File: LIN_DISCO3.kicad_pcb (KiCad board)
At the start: 2 copper layers, 48.9 x 34.9 mm, 20 parts, among them J1 CAR_STAT, J2 CAR_BAT, J3 WEBASTO, U1 PIC16F628-xxISO, U2 MCP1804x-5002xMB, U3 Si9243A

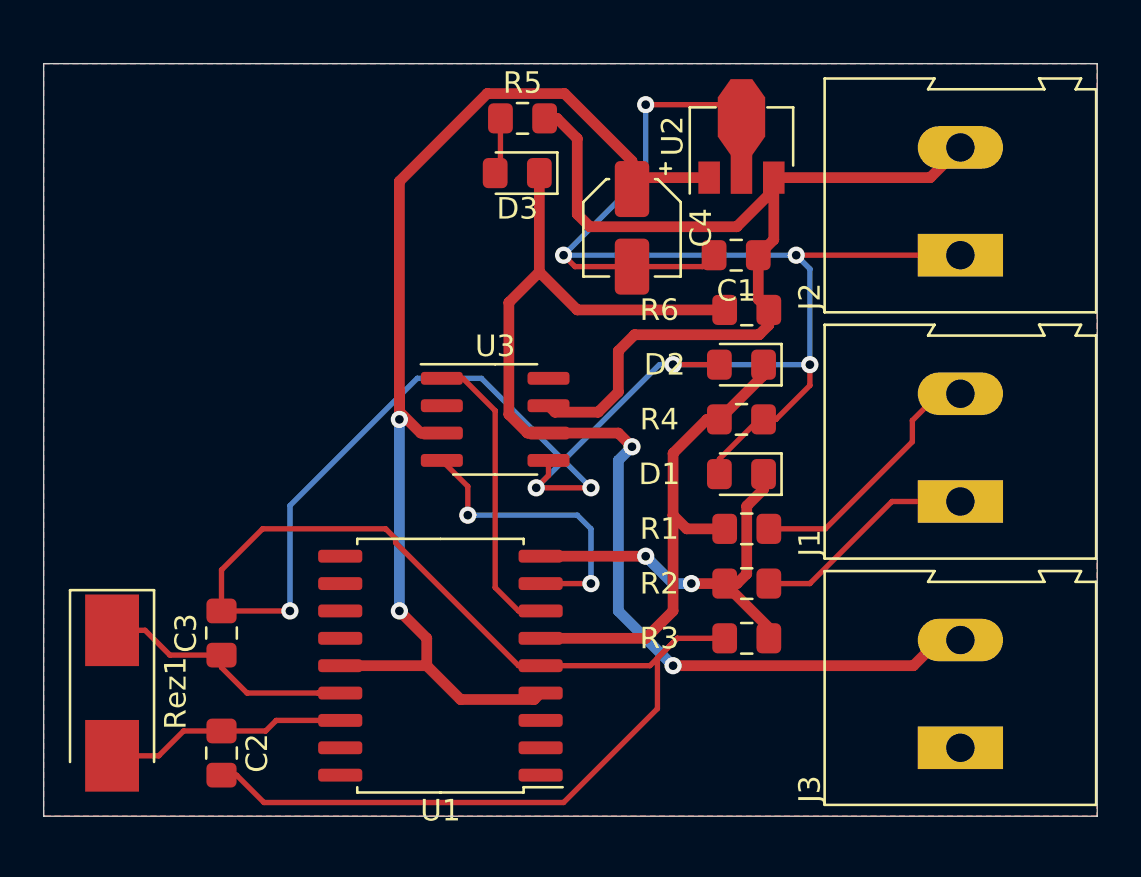
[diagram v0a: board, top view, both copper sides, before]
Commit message: reroute, added 6p arks
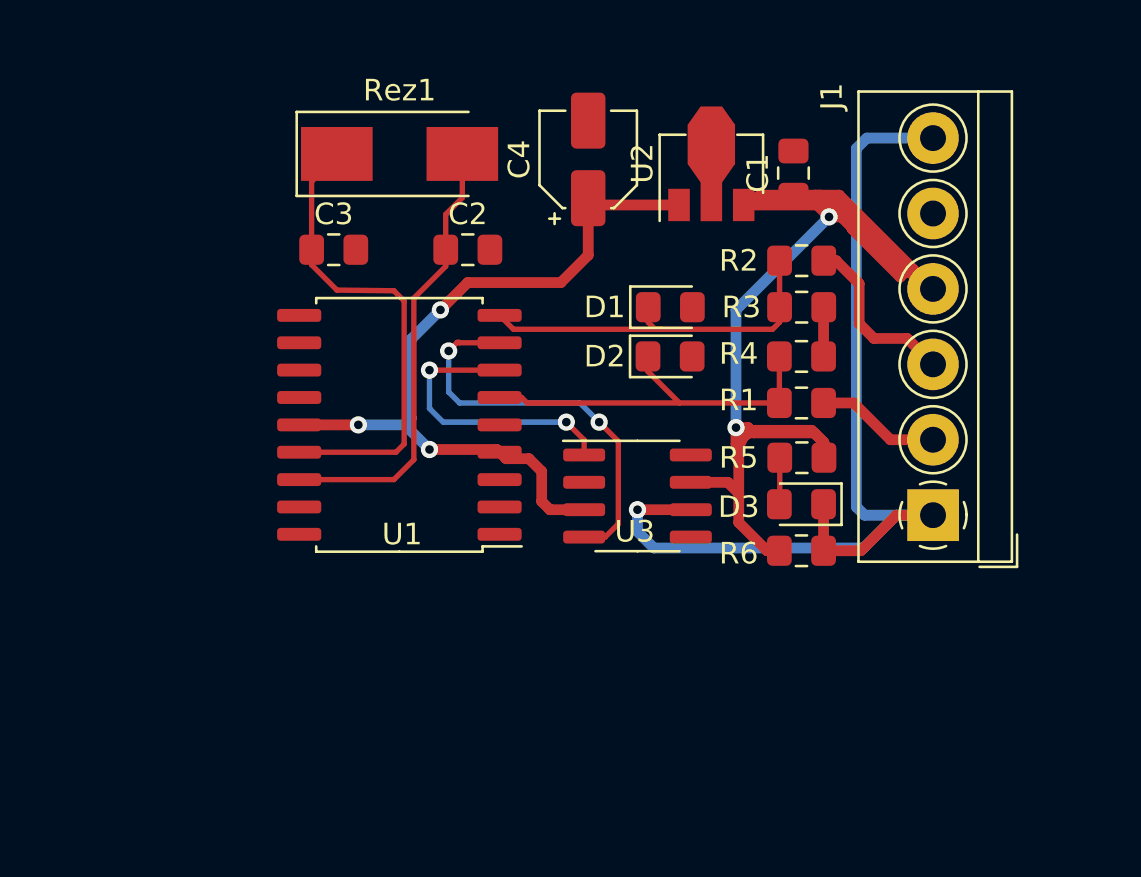
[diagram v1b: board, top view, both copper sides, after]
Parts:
- removed J2: CAR_BAT, TerminalBlock:TerminalBlock_Altech_AK300-2_P5.00mm
- removed J3: WEBASTO, TerminalBlock:TerminalBlock_Altech_AK300-2_P5.00mm
- J1: value CAR_STAT -> Conn_01x06_Female; footprint TerminalBlock:TerminalBlock_Altech_AK300-2_P5.00mm -> TerminalBlock_4Ucon:TerminalBlock_4Ucon_1x06_P3.50mm_Horizontal
- moved Rez1 28.4 mm to (165.7, 61.3), turned to 0 degrees
- moved C2 26.0 mm to (168.9, 65.8), turned to 0 degrees
- moved R5 20.4 mm to (184.4, 75.4)
- moved D3 20.3 mm to (184.4, 77.6)
- moved C3 18.5 mm to (162.7, 65.8), turned to 0 degrees
- moved R3 15.6 mm to (184.4, 68.5), turned to 0 degrees
- moved R2 15.2 mm to (184.4, 66.3)
- moved R6 11.5 mm to (184.4, 79.8), turned to 180 degrees
- moved U1 11.3 mm to (165.7, 73.9)
- moved D1 8.42 mm to (178.3, 68.5), turned to 0 degrees
- moved U3 7.50 mm to (176.8, 77.2)
- moved R1 6.37 mm to (184.4, 72.9)
- moved C1 4.65 mm to (184.0, 62.2), turned to 90 degrees
- moved R4 4.04 mm to (184.4, 70.7)
- moved C4 3.77 mm to (174.5, 61.6), turned to 90 degrees
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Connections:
- D1 pad 1: IGNITION -> RB3
- D2 pad 1: LOW_BEAM -> RB0
- J1 pad 1: Net-(J1-Pad1) -> WBUS
- J1 pad 2: Net-(J1-Pad2) -> LOW_BEAM
- R1 pad 1: LOW_BEAM -> RB0
- R1 pad 2: Net-(J1-Pad2) -> LOW_BEAM
- R2 pad 1: IGNITION -> RB3
- R2 pad 2: Net-(J1-Pad1) -> IGNITION
- R3 pad 1: IGNITION -> RB3
- R4 pad 1: LOW_BEAM -> RB0
- U1 pad 6: LOW_BEAM -> RB0
- U1 pad 9: IGNITION -> RB3
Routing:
- net GND: track 155.1 -> 6.29 mm, vias 8 -> 0
- net Vcc: track 55.2 -> 36.6 mm, vias 2 -> 3
- net RB0: track 0.00 -> 18.0 mm
- net RB3: track 0.00 -> 17.7 mm
- net LOW_BEAM: track 22.8 -> 5.79 mm
- net VBAT: track 45.8 -> 59.9 mm, vias 0 -> 2
- net Net-(J1-Pad2): track 12.1 -> 0.00 mm
- net IGNITION: track 18.6 -> 8.15 mm, vias 2 -> 0
- net Net-(J1-Pad1): track 10.5 -> 0.00 mm
- net Net-(C3-Pad1): track 12.1 -> 22.3 mm
- net Net-(C2-Pad1): track 11.3 -> 20.8 mm
- net WLINE_TX: track 13.9 -> 18.9 mm
- net WBUS: track 52.8 -> 50.2 mm, vias 2 -> 1
- net WLINE_RX: track 13.9 -> 13.5 mm, vias 0 -> 2
- removed copper zone on B.Cu, net GND
- removed copper zone on F.Cu, net GND
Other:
- board outline removed

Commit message: reroute: voltages
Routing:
- net GND: track 6.29 -> 113.0 mm, vias 0 -> 4
- net WBUS: track 50.2 -> 48.2 mm
- net Vcc: track 36.6 -> 37.6 mm
- added copper zone on B.Cu, net GND
- added copper zone on F.Cu, net GND
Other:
- board outline added: 35.6 x 22.6 mm

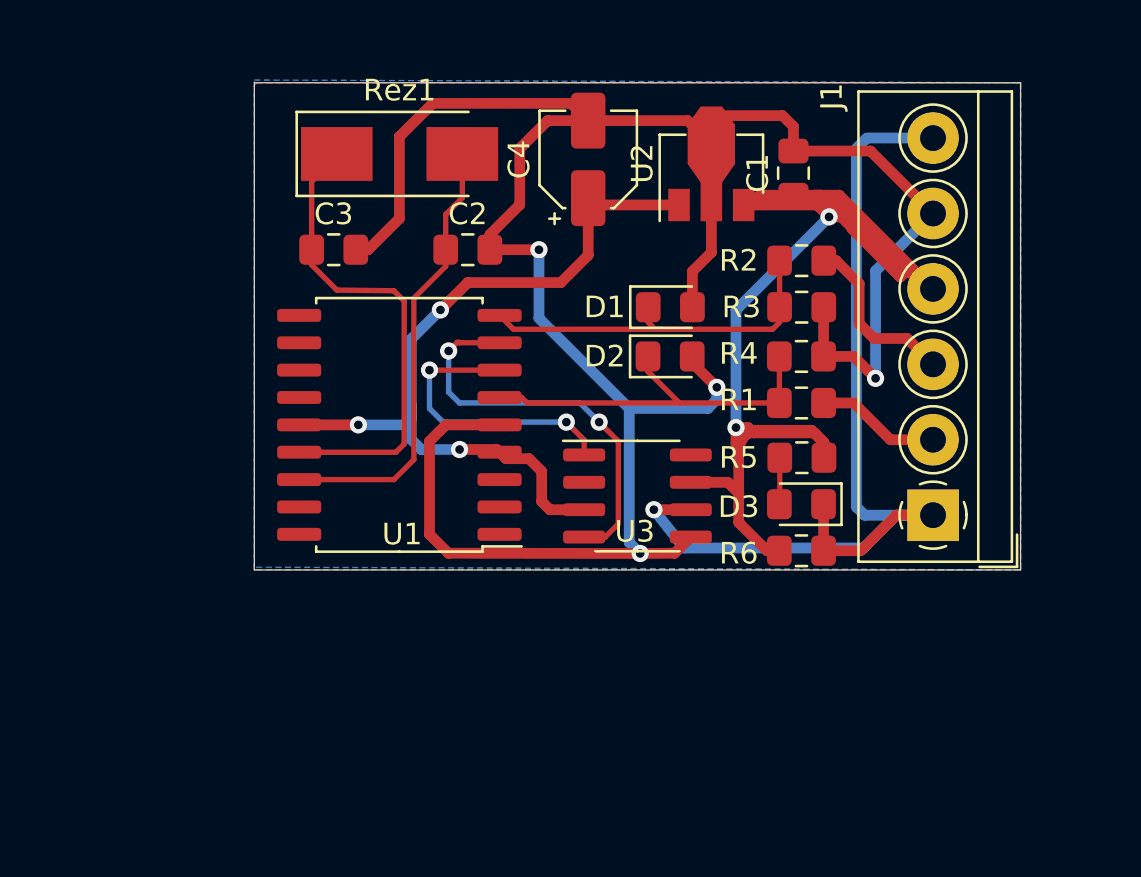
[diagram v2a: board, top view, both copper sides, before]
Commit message: added ICSP port
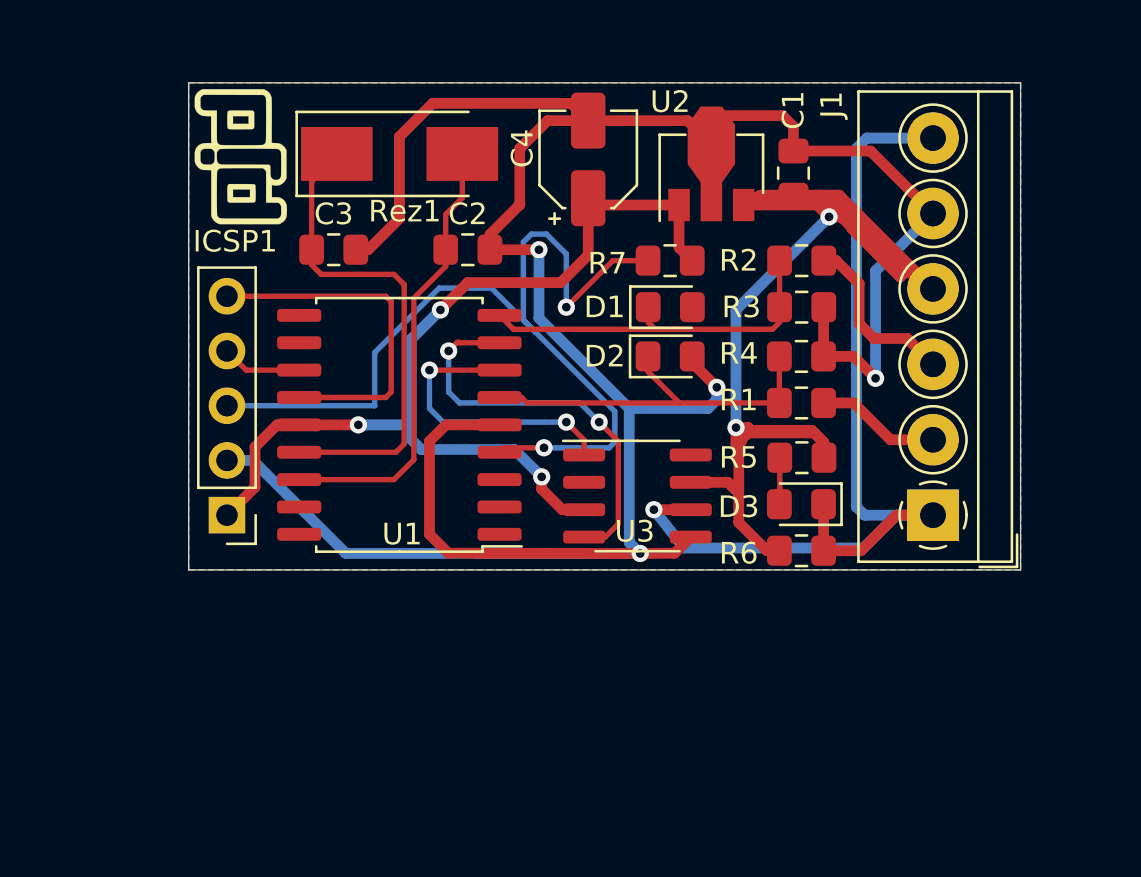
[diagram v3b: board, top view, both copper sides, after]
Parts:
- added G***: LOGO, logo:pjd_icon, F.Cu at (158.4, 61.5)
- added ICSP1: Conn_01x05_Male, Connector_PinHeader_2.54mm:PinHeader_1x05_P2.54mm_Vertical, F.Cu at (157.7, 78.1)
- added R7: 10k, Resistor_SMD:R_0805_2012Metric_Pad1.15x1.40mm_HandSolder, F.Cu at (178.3, 66.3)
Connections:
- U1 pad 12: Net-(U1-Pad12) -> CLK
- U1 pad 13: Net-(U1-Pad13) -> DATA_IO
- U1 pad 4: Vcc -> Vpp
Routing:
- net Vpp: track 0.00 -> 45.1 mm, vias 0 -> 2
- net DATA_IO: track 0.00 -> 16.3 mm
- net GND: track 113.0 -> 128.7 mm
- net Vcc: track 37.6 -> 46.2 mm
- net CLK: track 0.00 -> 3.72 mm
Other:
- board size 35.6 x 22.6 mm -> 38.6 x 22.6 mm
- board text added: "26.01.22"
- board text added: "CLK"
- board text added: "DATA_IO"
- board text added: "GND"
- board text added: "Gnd"
- board text added: "IGNITION"
- board text added: "LOW_BEAM"
- board text added: "VBAT"
- board text added: "Vcc"
- board text added: "Vpp"
- board text added: "WBUS"

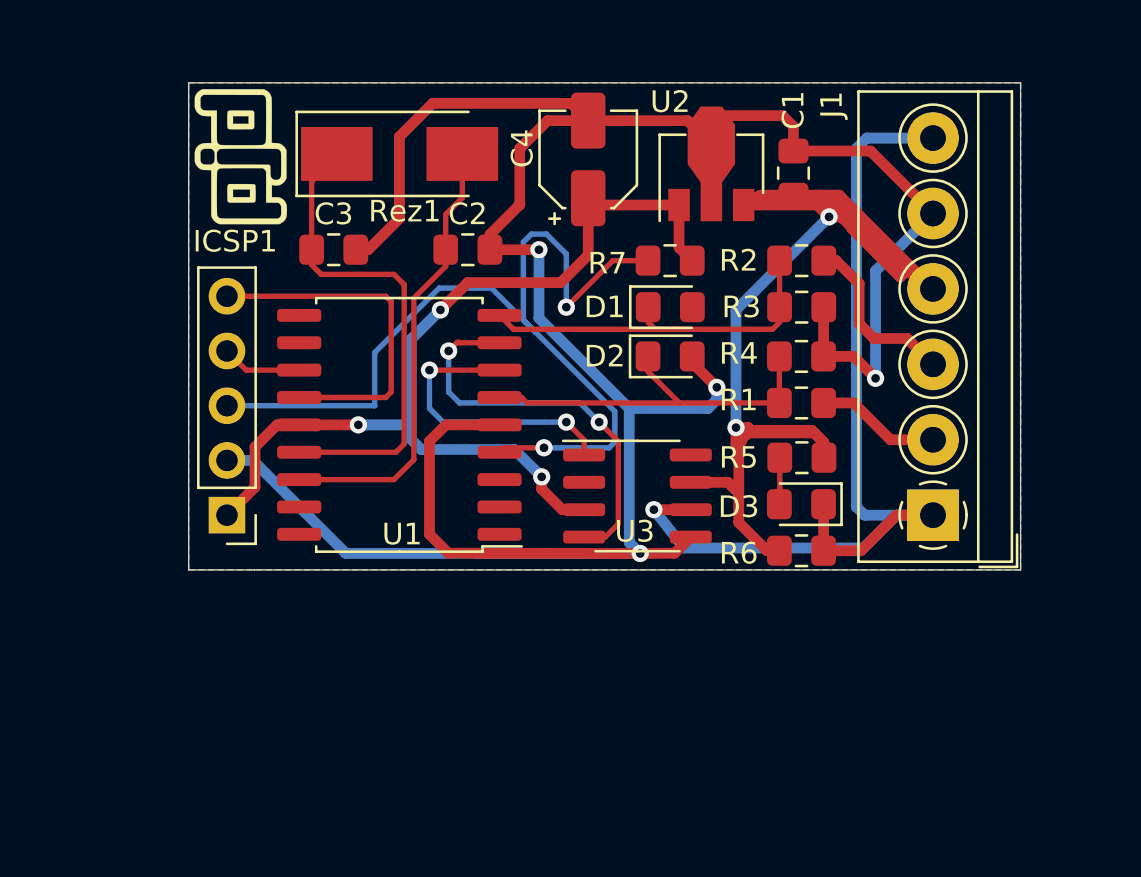
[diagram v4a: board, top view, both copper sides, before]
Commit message: updated board for sot23 and miniMELF
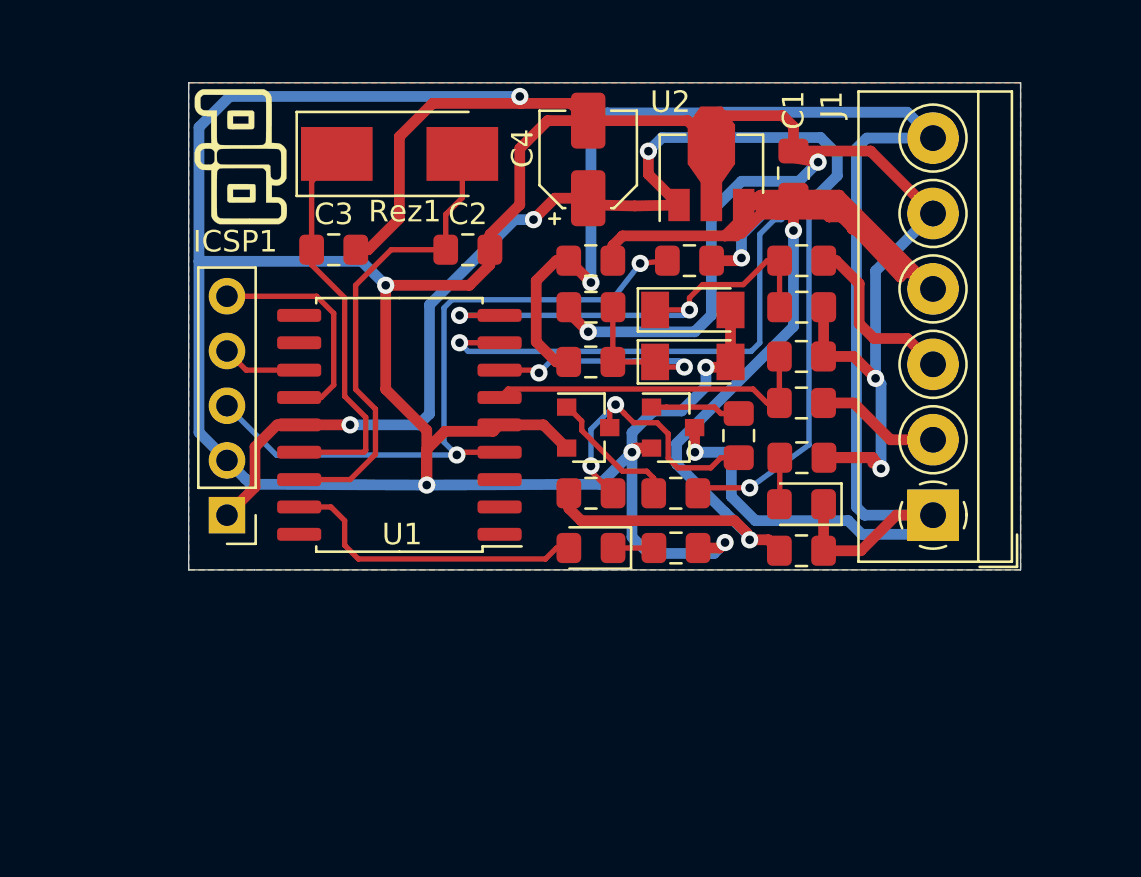
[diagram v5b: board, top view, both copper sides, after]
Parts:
- removed D2: D_Zener_5V6, Diode_SMD:D_0805_2012Metric_Pad1.15x1.40mm_HandSolder
- removed U3: Si9243A, Package_SO:SOIC-8_3.9x4.9mm_P1.27mm
- added D4: D_Zener_5V6, Diode_SMD:D_MiniMELF, F.Cu at (179.4, 71.0)
- added D5: LED, LED_SMD:LED_0805_2012Metric_Pad1.15x1.40mm_HandSolder, F.Cu at (174.6, 79.6)
- added Q1: BC847, Package_TO_SOT_SMD:SOT-23, F.Cu at (174.5, 74.0)
- added Q2: BC847, Package_TO_SOT_SMD:SOT-23, F.Cu at (178.4, 74.0)
- added R10: 10K, Resistor_SMD:R_0805_2012Metric_Pad1.15x1.40mm_HandSolder, F.Cu at (181.5, 74.4)
- added R11: 10k, Resistor_SMD:R_0805_2012Metric_Pad1.15x1.40mm_HandSolder, F.Cu at (174.6, 71.0)
- added R12: 10K, Resistor_SMD:R_0805_2012Metric_Pad1.15x1.40mm_HandSolder, F.Cu at (174.6, 66.3)
- added R13: 2K, Resistor_SMD:R_0805_2012Metric_Pad1.15x1.40mm_HandSolder, F.Cu at (178.6, 79.6)
- added R6: 10K, Resistor_SMD:R_0805_2012Metric_Pad1.15x1.40mm_HandSolder, F.Cu at (178.6, 77.1)
- added R8: 10K, Resistor_SMD:R_0805_2012Metric_Pad1.15x1.40mm_HandSolder, F.Cu at (174.6, 77.1)
- added R9: 10k, Resistor_SMD:R_0805_2012Metric_Pad1.15x1.40mm_HandSolder, F.Cu at (174.6, 68.5)
- D1: footprint Diode_SMD:D_0805_2012Metric_Pad1.15x1.40mm_HandSolder -> Diode_SMD:D_MiniMELF
- moved D1 1.05 mm to (179.4, 68.6)
- moved R7 0.90 mm to (179.2, 66.3)
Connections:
- R5 pad 2: VBAT -> GND
- U1 pad 17: Net-(U1-Pad17) -> W_ACTIVE
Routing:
- net GND: track 128.7 -> 199.2 mm, vias 4 -> 10
- net WBUS: track 48.2 -> 79.2 mm, vias 1 -> 2
- net WLINE_TX: track 18.9 -> 40.3 mm
- net VBAT: track 59.9 -> 76.1 mm
- net W_ACTIVE: track 0.00 -> 14.4 mm
- net Net-(Q1-Pad3): track 0.00 -> 13.8 mm, vias 0 -> 2
- net Vpp: track 45.1 -> 32.1 mm
- net Vcc: track 46.2 -> 52.9 mm, vias 3 -> 4
- net Net-(Q1-Pad1): track 0.00 -> 6.36 mm
- net DATA_IO: track 16.3 -> 10.5 mm
- net Net-(C3-Pad1): track 22.7 -> 18.4 mm
- net RB3: track 17.7 -> 21.8 mm, vias 0 -> 2
- net Net-(Q2-Pad1): track 0.00 -> 4.04 mm
- net WLINE_RX: track 13.5 -> 17.2 mm
- net RB0: track 18.0 -> 15.6 mm
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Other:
- board text added: "15.02.22"
- board text removed: "26.01.22"

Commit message: board layout prepared for production
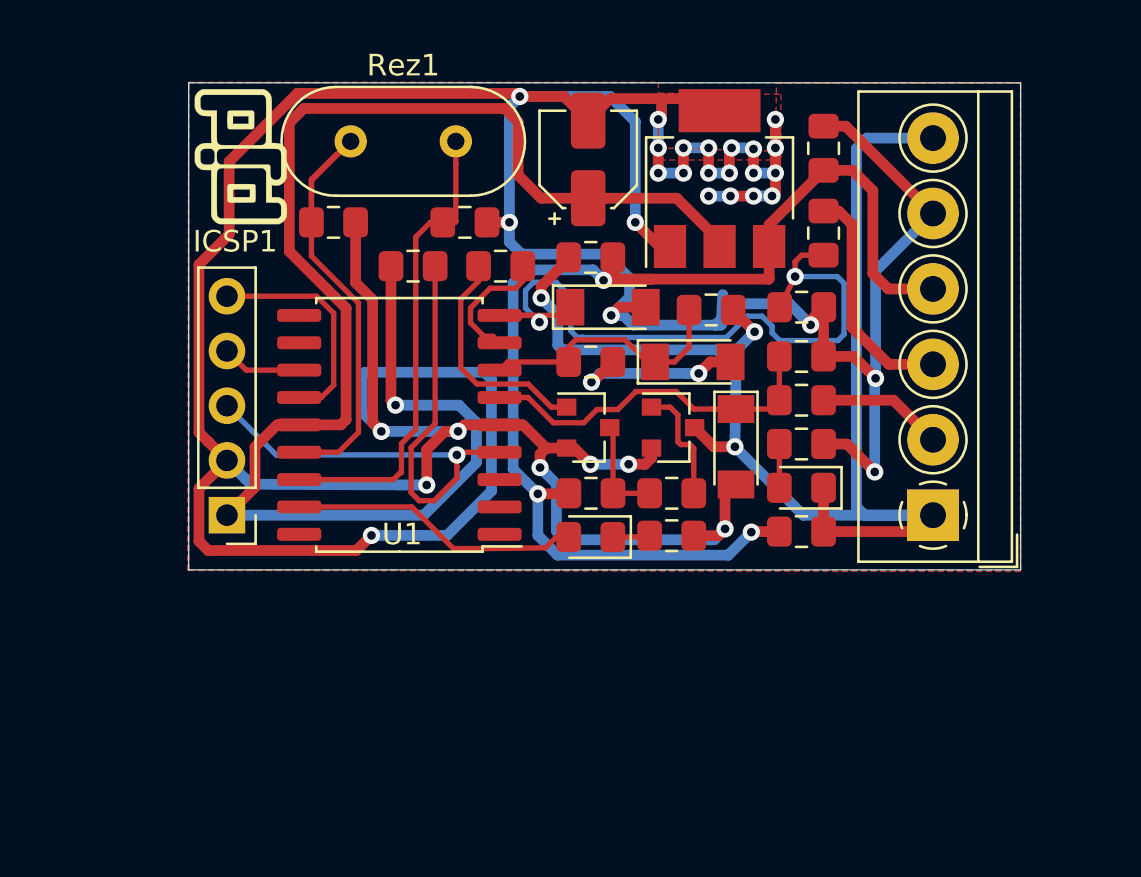
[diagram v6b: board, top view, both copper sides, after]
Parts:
- added D2: D_Zener_5V6, Diode_SMD:D_MiniMELF, F.Cu at (181.4, 74.9)
- Rez1: footprint Crystal:Crystal_SMD_0603-2Pin_6.0x3.5mm_HandSoldering -> Crystal:Crystal_HC49-U_Vertical
- U2: value MCP1804x-5002xMB -> MCP1754S-5002xCB; footprint Package_TO_SOT_SMD:SOT-89-3 -> Package_TO_SOT_SMD:SOT-223
- moved R6 13.3 mm to (170.4, 66.5)
- moved R7 12.8 mm to (166.4, 66.5), turned to 0 degrees
- moved R11 6.09 mm to (180.2, 68.6), turned to 180 degrees
- moved R10 4.10 mm to (178.4, 77.1), turned to 180 degrees
- moved D1 3.94 mm to (175.4, 68.5)
- moved R9 2.54 mm to (174.6, 71.0), turned to 0 degrees
- moved Rez1 2.34 mm to (163.5, 60.8)
- moved C1 1.81 mm to (185.4, 61.1)
- moved R2 1.63 mm to (185.4, 65.0), turned to 90 degrees
- moved C2 1.28 mm to (168.8, 64.5)
- moved C3 1.27 mm to (162.7, 64.5)
- moved R6 0.89 mm to (184.4, 78.9)
- moved D3 0.76 mm to (184.4, 76.8)
- moved R5 0.64 mm to (184.4, 74.8)
- moved R13 0.61 mm to (178.4, 79.1)
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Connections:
- U2 pad 1: Vcc -> GND
- U2 pad 2: GND -> Vcc
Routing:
- net WLINE_TX: track 40.3 -> 6.06 mm, vias 2 -> 0
- net GND: track 199.2 -> 229.9 mm, vias 10 -> 35
- net Vcc: track 52.9 -> 72.9 mm, vias 4 -> 1
- net VBAT: track 76.1 -> 56.4 mm, vias 2 -> 3
- net WBUS: track 79.2 -> 65.2 mm, vias 2 -> 3
- net RB3: track 21.8 -> 33.8 mm
- net Net-(Q1-Pad3): track 13.8 -> 4.81 mm, vias 2 -> 0
- net WLINE_RX: track 17.2 -> 12.2 mm, vias 2 -> 0
- net Net-(Q1-Pad1): track 6.36 -> 10.7 mm
- net Vpp: track 32.1 -> 28.4 mm, vias 2 -> 1
- net Net-(C3-Pad1): track 18.4 -> 22.0 mm
- net IGNITION: track 8.15 -> 11.6 mm
- net Net-(Q2-Pad1): track 4.04 -> 5.57 mm
- net RB0: track 15.6 -> 16.6 mm
- net W_ACTIVE: track 14.4 -> 13.5 mm
